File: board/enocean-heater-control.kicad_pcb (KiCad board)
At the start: 4 copper layers, 138 x 85 mm, 43 parts, among them J1 USB_C_Receptacle_PowerOnly_6P, J109 DBG_UART, J401 DBG, J601 Conn_01x08, J602 Conn_01x08, J603 Conn_01x08, J604 Conn_01x08, J605 Conn_01x08, J606 Conn_01x08, J607 Conn_01x08, J608 Conn_01x08, SW501 RST, U101 LM317AEMP, U301 ATSAML21G18B-AUT, Y301 32768Hz

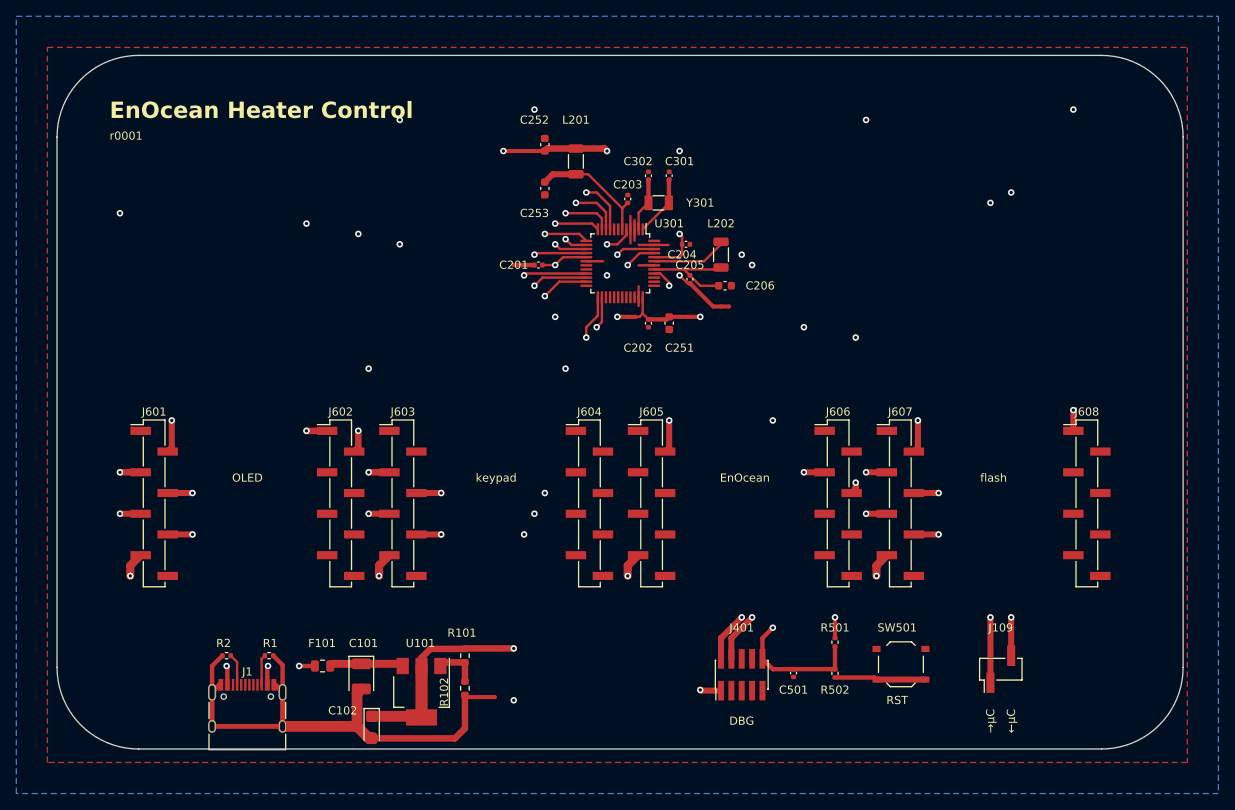
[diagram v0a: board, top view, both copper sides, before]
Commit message: redo board with STM32G0B0CET
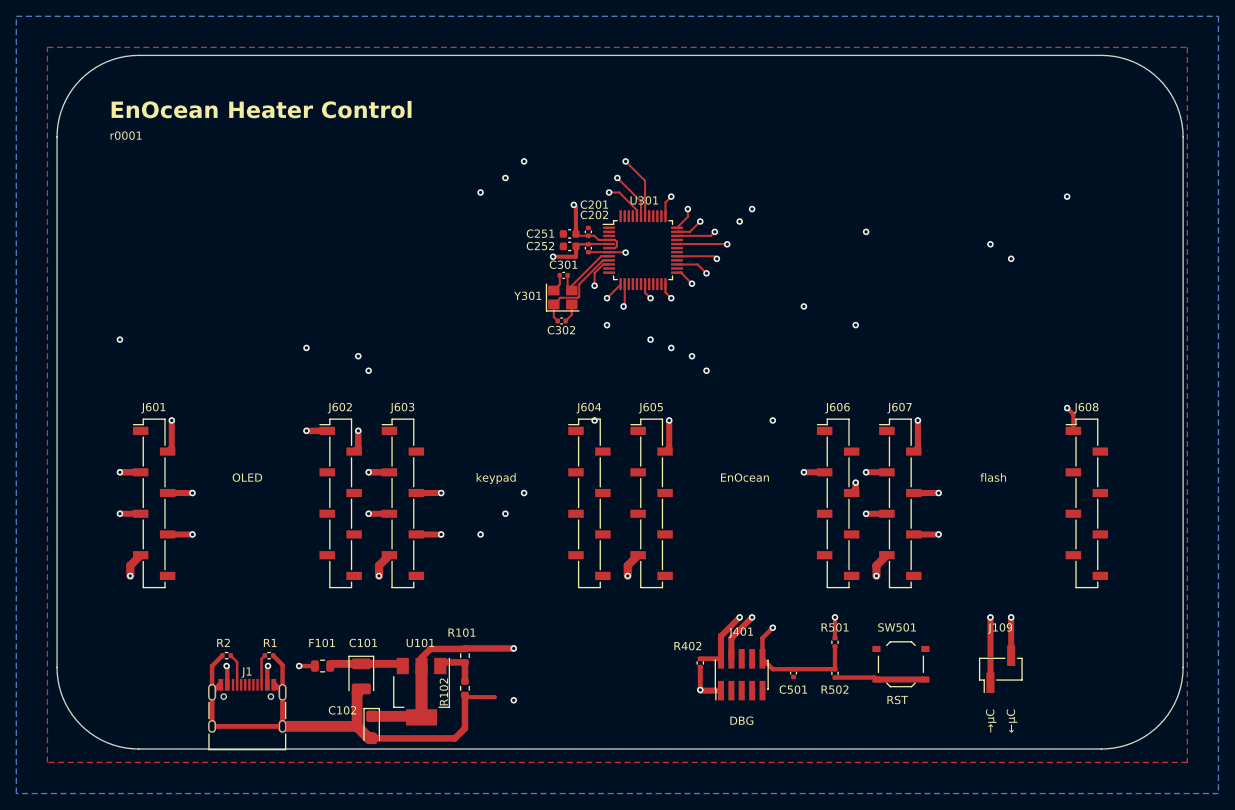
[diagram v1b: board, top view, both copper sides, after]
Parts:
- removed C203, C204, C205: 100nF, Capacitor_SMD:C_0402_1005Metric
- removed C206: 1µF, Capacitor_SMD:C_0603_1608Metric
- removed C253: 10µF, Capacitor_SMD:C_0603_1608Metric
- removed L201, L202: 10µH, Inductor_SMD:L_1206_3216Metric
- removed NT203, NT204: NetTie_2, NetTie:NetTie-2_SMD_Pad0.5mm
- added R402: 100kΩ, Resistor_SMD:R_0402_1005Metric, F.Cu at (163.8, 108.5)
- C251: value 10µF -> 4.7µF
- C252: value 10µF -> 1µF
- C301, C302: value 22pF -> 20pF
- J109: value DBG_UART -> Conn_01x02
- J601, J602, J603, J604, J605, J606, J607, J608: footprint Connector_PinHeader_2.54mm:PinHeader_1x08_P2.54mm_Vertical_SMD_Pin1Left -> Connector_PinSocket_2.54mm:PinSocket_1x08_P2.54mm_Vertical_SMD_Pin1Left
- U301: value ATSAML21G18B-AUT -> STM32G0B0KETx; footprint Package_QFP:TQFP-48_7x7mm_P0.5mm -> Package_QFP:LQFP-48_7x7mm_P0.5mm
- Y301: value 32768Hz -> 16MHz; footprint Crystal:Crystal_SMD_3215-2Pin_3.2x1.5mm -> Crystal:Crystal_SMD_3225-4Pin_3.2x2.5mm
- moved C302 20.7 mm to (146.8, 66.5), turned to 180 degrees
- moved NT201 18.0 mm to (148.6, 53.8), turned to 90 degrees
- moved C301 17.8 mm to (147.1, 61.0), turned to 180 degrees
- moved Y301 16.5 mm to (147.0, 63.7), turned to 0 degrees
- moved C251 16.4 mm to (147.8, 55.9), turned to 180 degrees
- moved C252 12.8 mm to (147.8, 57.4), turned to 180 degrees
- moved C202 11.8 mm to (150.1, 57.6)
- moved NT202 10.4 mm to (148.1, 58.7), turned to 0 degrees
- moved C201 7.35 mm to (150.1, 55.6), turned to 90 degrees
- moved U301 3.23 mm to (156.8, 57.9), turned to 0 degrees
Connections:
- C201 pad 1: /Microcontroller/VDDIO1 -> /Microcontroller/VDD
- C202 pad 1: /Microcontroller/VDDIO2 -> /Microcontroller/VREF+
- C251 pad 1: /Microcontroller/VDDIO2 -> /Microcontroller/VDD
- C252 pad 1: /Microcontroller/VDDIN -> /Microcontroller/VREF+
- C301 pad 1: /Microcontroller/Clock/MCUXIN -> /Microcontroller/Clock/MCU_OSC_IN
- C302 pad 2: /Microcontroller/Clock/MCUXOUT -> /Microcontroller/Clock/MCU_OSC_OUT
- NT201 pad 1: /Microcontroller/VDDIO2 -> /Microcontroller/VDD
- NT202 pad 1: /Microcontroller/VDDIO2 -> /+3.3V
- NT202 pad 2: /Microcontroller/VDDIO1 -> /Microcontroller/VREF+
- U301 pad 1: /Microcontroller/Clock/MCUXIN -> unconnected-(U301-PC13-Pad1)
- U301 pad 10: /Microcontroller/DBG_UART_MCURX -> /~{RST}
- U301 pad 11: /OLED_~{CS} -> unconnected-(U301-PA0-Pad11)
- U301 pad 12: /OLED_D_~{C} -> unconnected-(U301-PA1-Pad12)
- U301 pad 13: /OLED_EN -> /ENO_C2P
- U301 pad 14: /KPAD_~{CS} -> /ENO_P2C
- U301 pad 15: /FLASH_~{CS} -> unconnected-(U301-PA4-Pad15)
- U301 pad 16: /FLASH_~{WP} -> unconnected-(U301-PA5-Pad16)
- U301 pad 17: /Microcontroller/VDDIO1 -> unconnected-(U301-PA6-Pad17)
- U301 pad 18: /GND -> unconnected-(U301-PA7-Pad18)
- U301 pad 19: unconnected-(U301-PB10-Pad19) -> /OLED_~{CS}
- U301 pad 2: /Microcontroller/Clock/MCUXOUT -> unconnected-(U301-PC14-Pad2)
- U301 pad 21: /COPI -> unconnected-(U301-PB2-Pad21)
- U301 pad 22: /CIPO -> unconnected-(U301-PB10-Pad22)
- U301 pad 23: /SCK -> unconnected-(U301-PB11-Pad23)
- U301 pad 24: unconnected-(U301-PA15-Pad24) -> /OLED_D_~{C}
- U301 pad 25: /ENO_C2P -> /OLED_EN
- U301 pad 26: /ENO_P2C -> unconnected-(U301-PB14-Pad26)
- U301 pad 27: unconnected-(U301-PA18-Pad27) -> /KPAD_~{CS}
- U301 pad 29: unconnected-(U301-PA20-Pad29) -> /Microcontroller/DBG_UART_MCUTX
- U301 pad 3: /GND -> unconnected-(U301-PC15-Pad3)
- U301 pad 32: unconnected-(U301-PA23-Pad32) -> /Microcontroller/DBG_UART_MCURX
- U301 pad 34: unconnected-(U301-PA25-Pad34) -> /FLASH_~{CS}
- U301 pad 35: /GND -> /Microcontroller/Debug/SWDIO
- U301 pad 36: /Microcontroller/VDDIO2 -> /Microcontroller/Debug/SWCLK
- U301 pad 37: unconnected-(U301-PB22-Pad37) -> /FLASH_~{WP}
- U301 pad 4: /GND -> /Microcontroller/VDD
- U301 pad 40: /~{RST} -> unconnected-(U301-PD2-Pad40)
- U301 pad 41: /Microcontroller/VDDCORE -> unconnected-(U301-PD3-Pad41)
- U301 pad 42: /GND -> /SCK
- U301 pad 43: /Microcontroller/VSW -> /CIPO
- U301 pad 44: /Microcontroller/VDDIN -> /COPI
- U301 pad 45: /Microcontroller/Debug/SWCLK -> unconnected-(U301-PB6-Pad45)
- U301 pad 46: /Microcontroller/Debug/SWDIO -> unconnected-(U301-PB7-Pad46)
- U301 pad 47: /GND -> unconnected-(U301-PB8-Pad47)
- U301 pad 48: /GND -> unconnected-(U301-PB9-Pad48)
- U301 pad 5: /Microcontroller/GNDANA -> /Microcontroller/VREF+
- U301 pad 6: /Microcontroller/VDDANA -> /Microcontroller/VDD
- U301 pad 7: unconnected-(U301-PB08-Pad7) -> /GND
- U301 pad 8: unconnected-(U301-PB09-Pad8) -> /Microcontroller/Clock/MCU_OSC_IN
- U301 pad 9: /Microcontroller/DBG_UART_MCUTX -> /Microcontroller/Clock/MCU_OSC_OUT
- Y301 pad 1: /Microcontroller/Clock/MCUXOUT -> /Microcontroller/Clock/MCU_OSC_OUT
- Y301 pad 2: /Microcontroller/Clock/MCUXIN -> /GND
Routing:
- net /FLASH_~{CS}: track 141.2 -> 55.4 mm, vias 5 -> 3
- net /FLASH_~{WP}: track 129.6 -> 80.0 mm, vias 4 -> 3
- net /Microcontroller/VDDIN: track 35.7 -> 0.00 mm, vias 3 -> 0
- net /SCK: track 130.5 -> 161.4 mm, vias 5 -> 6
- net /CIPO: track 133.8 -> 159.8 mm, vias 5 -> 6
- net /Microcontroller/DBG_UART_MCUTX: track 115.3 -> 89.7 mm
- net /Microcontroller/DBG_UART_MCURX: track 115.9 -> 91.9 mm
- net /COPI: track 140.0 -> 163.3 mm, vias 5 -> 6
- net /Microcontroller/GNDANA: track 22.9 -> 0.00 mm, vias 3 -> 0
- net /Microcontroller/VDDIO1: track 21.0 -> 0.00 mm, vias 3 -> 0
- net /Microcontroller/VDDANA: track 15.1 -> 0.00 mm
- net /KPAD_~{CS}: track 58.0 -> 72.4 mm
- net /Microcontroller/VDDCORE: track 13.0 -> 0.00 mm
- net /Microcontroller/Clock/MCU_OSC_OUT: track 0.00 -> 12.1 mm
- net /GND: track 18.5 -> 9.10 mm, vias 1 -> 2
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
